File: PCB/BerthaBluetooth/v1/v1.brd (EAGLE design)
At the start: 111.9 x 84.6 mm, 112 parts, among them CON1 SPI, IC1 REG1117, J1 RJ12, J2 RJ12, J3 RJ12, J4 RJ12, J5 RJ12, J6 RJ12, Q1 BSP613P, Q10 BSP613P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

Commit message: Update labels
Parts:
- Q1, Q10, Q2, Q3, Q4, Q5, Q6, Q8, Q9: value BSP613P -> BSP75
- R25, R33, R5: value RJ12 -> 1k
- X4: value MINI-USB-SCHIELD-32005-201 -> MINI-USB

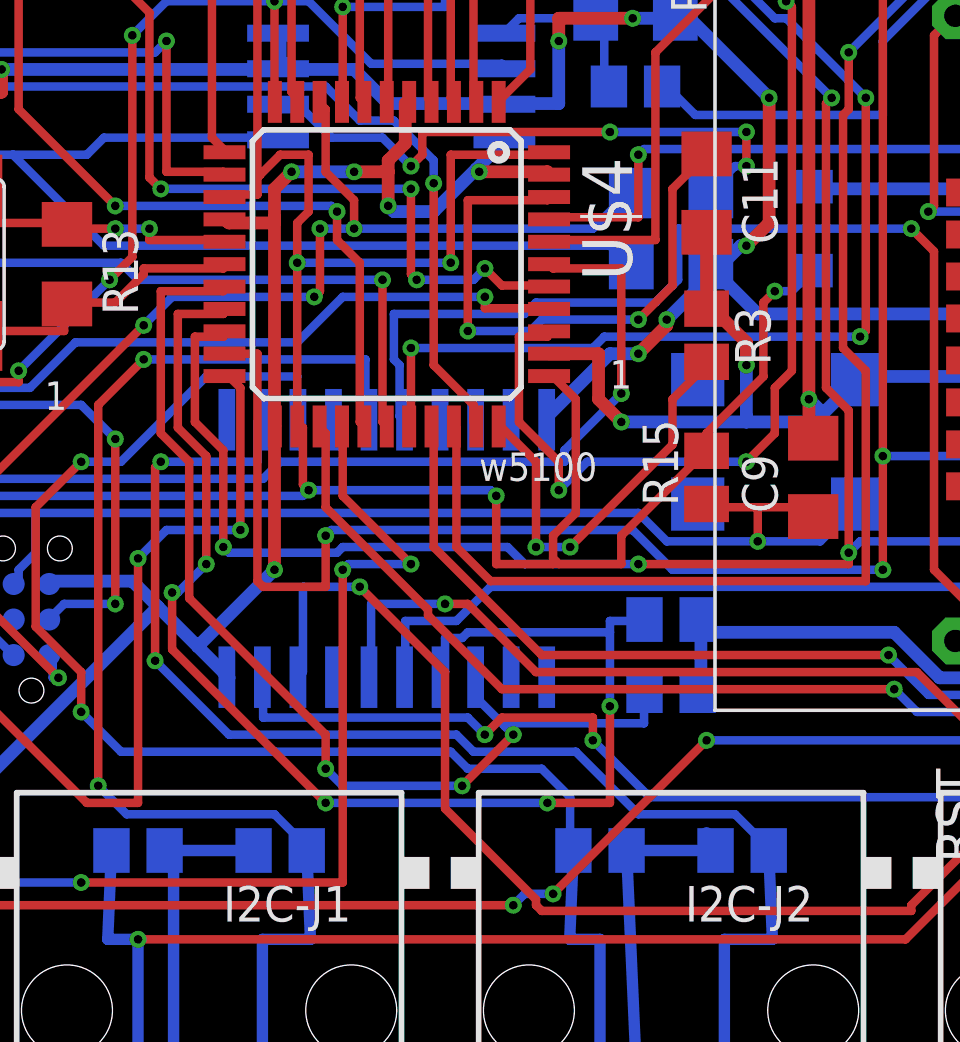
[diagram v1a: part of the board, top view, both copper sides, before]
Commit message: Update labels of sensor
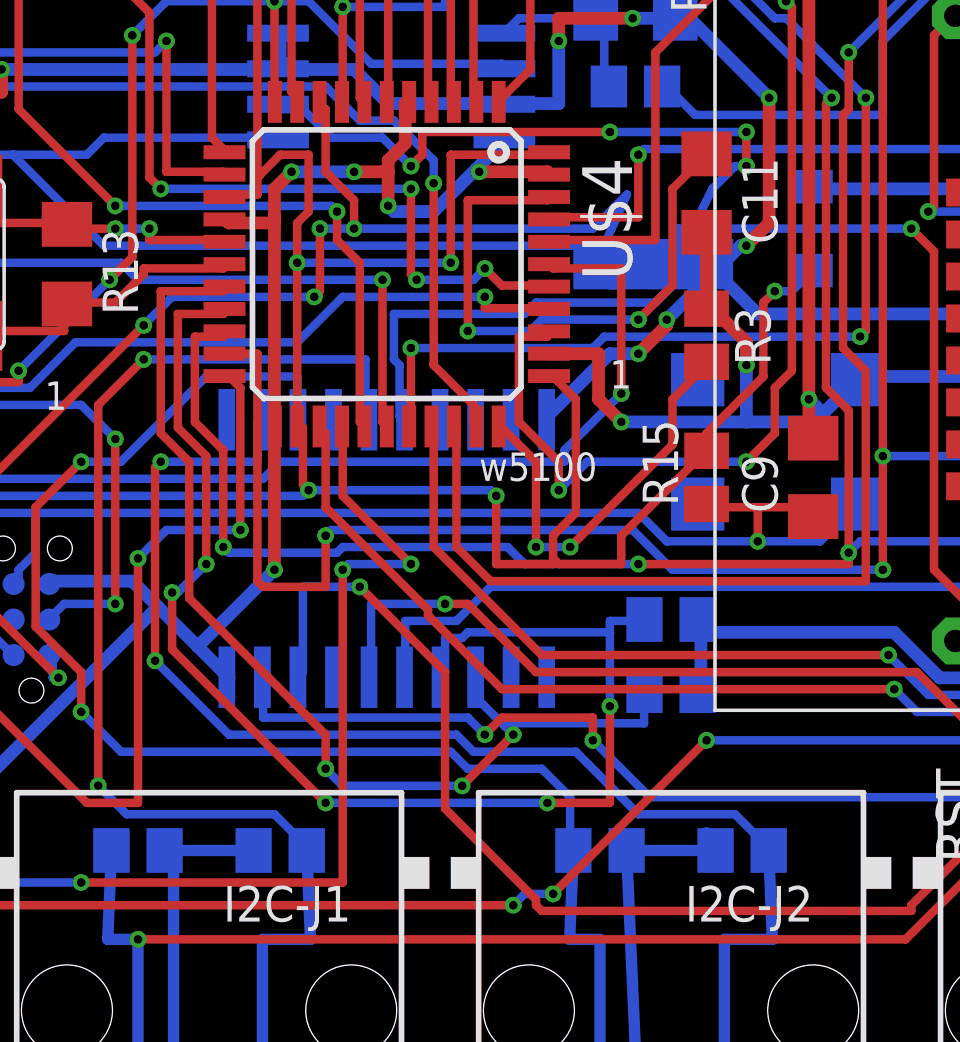
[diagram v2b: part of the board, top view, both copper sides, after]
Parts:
- moved R18 2.84 mm to (63.5, 39.4)
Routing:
- net N$23: track 21.6 -> 24.5 mm
- net SCK: track 40.6 -> 43.2 mm
- net +5V: track 659.8 -> 659.2 mm
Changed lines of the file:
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@@
 <layer number="23" name="tOrigins" color="15" fill="1" visible="yes" active="yes"/>
 <layer number="24" name="bOrigins" color="15" fill="1" visible="yes" active="yes"/>
-<layer number="25" name="tNames" color="7" fill="1" visible="no" active="yes"/>
-<layer number="26" name="bNames" color="7" fill="1" visible="no" active="yes"/>
-<layer number="27" name="tValues" color="7" fill="1" visible="no" active="yes"/>
+<layer number="25" name="tNames" color="7" fill="1" visible="yes" active="yes"/>
+<layer number="26" name="bNames" color="7" fill="1" visible="yes" active="yes"/>
+<layer number="27" name="tValues" color="7" fill="1" visible="yes" active="yes"/>
 <layer number="28" name="bValues" color="7" fill="1" visible="yes" active="yes"/>
-<layer number="29" name="tStop" color="7" fill="3" visible="no" active="yes"/>
-<layer number="30" name="bStop" color="7" fill="6" visible="no" active="yes"/>
-<layer number="31" name="tCream" color="7" fill="4" visible="no" active="yes"/>
-<layer number="32" name="bCream" color="7" fill="5" visible="no" active="yes"/>
-<layer number="33" name="tFinish" color="6" fill="3" visible="no" active="yes"/>
+<layer number="29" name="tStop" color="7" fill="3" visible="yes" active="yes"/>
+<layer number="30" name="bStop" color="7" fill="6" visible="yes" active="yes"/>
+<layer number="31" name="tCream" color="7" fill="4" visible="yes" active="yes"/>
+<layer number="32" name="bCream" color="7" fill="5" visible="yes" active="yes"/>
+<layer number="33" name="tFinish" color="6" fill="3" visible="yes" active="yes"/>
 <layer number="34" name="bFinish" color="6" fill="6" visible="yes" active="yes"/>
-<layer number="35" name="tGlue" color="7" fill="4" visible="no" active="yes"/>
-<layer number="36" name="bGlue" color="7" fill="5" visible="no" active="yes"/>
-<layer number="37" name="tTest" color="7" fill="1" visible="no" active="yes"/>
-<layer number="38" name="bTest" color="7" fill="1" visible="no" active="yes"/>
-<layer number="39" name="tKeepout" color="4" fill="11" visible="no" active="yes"/>
-<layer number="40" name="bKeepout" color="1" fill="11" visible="no" active="yes"/>
+<layer number="35" name="tGlue" color="7" fill="4" visible="yes" active="yes"/>
+<layer number="36" name="bGlue" color="7" fill="5" visible="yes" active="yes"/>
+<layer number="37" name="tTest" color="7" fill="1" visible="yes" active="yes"/>
+<layer number="38" name="bTest" color="7" fill="1" visible="yes" active="yes"/>
+<layer number="39" name="tKeepout" color="4" fill="11" visible="yes" active="yes"/>
+<layer number="40" name="bKeepout" color="1" fill="11" visible="yes" active="yes"/>
 <layer number="41" name="tRestrict" color="4" fill="10" visible="yes" active="yes"/>
 <layer number="42" name="bRestrict" color="1" fill="10" visible="yes" active="yes"/>
@@
 <layer number="45" name="Holes" color="7" fill="1" visible="no" active="yes"/>
 <layer number="46" name="Milling" color="3" fill="1" visible="no" active="yes"/>
-<layer number="47" name="Measures" color="7" fill="1" visible="no" active="yes"/>
-<layer number="48" name="Document" color="7" fill="1" visible="no" active="yes"/>
-<layer number="49" name="Reference" color="7" fill="1" visible="no" active="yes"/>
+<layer number="47" name="Measures" color="7" fill="1" visible="yes" active="yes"/>
+<layer number="48" name="Document" color="7" fill="1" visible="yes" active="yes"/>
+<layer number="49" name="Reference" color="7" fill="1" visible="yes" active="yes"/>
 <layer number="50" name="dxf" color="12" fill="1" visible="no" active="no"/>
-<layer number="51" name="tDocu" color="7" fill="1" visible="no" active="yes"/>
+<layer number="51" name="tDocu" color="7" fill="1" visible="yes" active="yes"/>
 <layer number="52" name="bDocu" color="7" fill="1" visible="yes" active="yes"/>
 <layer number="53" name="tGND_GNDA" color="7" fill="1" visible="no" active="no"/>
@@
 <attribute name="VALUE" x="64.77" y="44.7675" size="1.27" layer="28" rot="MR90"/>
 </element>
-<element name="R18" library="rcl" package="R1206" value="10k" x="64.77" y="41.91" smashed="yes" rot="MR180">
-<attribute name="NAME" x="63.5" y="40.64" size="1.27" layer="26" rot="MR180"/>
-<attribute name="VALUE" x="66.675" y="41.275" size="1.27" layer="28" rot="MR90"/>
+<element name="R18" library="rcl" package="R1206" value="10k" x="63.5" y="39.37" smashed="yes" rot="MR180">
+<attribute name="NAME" x="62.23" y="38.1" size="1.27" layer="26" rot="MR180"/>
+<attribute name="VALUE" x="65.405" y="38.735" size="1.27" layer="28" rot="MR90"/>
 </element>
 <element name="R" library="rcl" package="R0805" value="1k" x="23.495" y="76.2" rot="MR90"/>
@@
 <element name="R9" library="rcl" package="R0805" value="1.2K" x="72.39" y="50.8" rot="R270"/>
 <element name="R10" library="rcl" package="R0805" value="1K" x="63.5" y="50.8" rot="R270"/>
-<element name="C11" library="rcl" package="C1206" value="100nF" x="66.04" y="41.91" rot="R270"/>
+<element name="C11" library="rcl" package="C1206" value="100nF" x="66.04" y="41.91" smashed="yes" rot="R270">
+<attribute name="NAME" x="67.31" y="43.18" size="1.27" layer="25" rot="R270"/>
+<attribute name="VALUE" x="62.23" y="44.45" size="1.27" layer="27" rot="R270"/>
+</element>
 <element name="CON1" library="lpatiny" package="TC2030-MCP-NL" value="SPI" x="41.91" y="24.13" rot="MR90"/>
 <element name="C10" library="rcl" package="C1206" value="10uF" x="31.75" y="38.1" smashed="yes" rot="MR90">
@@
 </element>
 <element name="D5" library="lpatiny" package="LED-1206" value="1N581D1206" x="26.67" y="35.56" rot="MR180"/>
-<element name="R3" library="resistor" package="M0805" value="10k" x="66.04" y="36.83" rot="R270"/>
-<element name="R15" library="resistor" package="M0805" value="10k" x="66.04" y="31.75" rot="R90"/>
+<element name="R3" library="resistor" package="M0805" value="10k" x="66.04" y="36.83" smashed="yes" rot="R270">
+<attribute name="NAME" x="67.056" y="37.846" size="1.27" layer="25" rot="R270"/>
+<attribute name="VALUE" x="63.754" y="37.846" size="1.27" layer="27" rot="R270"/>
+</element>
+<element name="R15" library="resistor" package="M0805" value="10k" x="66.04" y="31.75" smashed="yes" rot="R90">
+<attribute name="NAME" x="65.024" y="30.734" size="1.27" layer="25" rot="R90"/>
+<attribute name="VALUE" x="64.8335" y="30.4165" size="1.27" layer="27" rot="R90"/>
+</element>
 <element name="C3" library="rcl" package="C1206" value="100nF" x="53.34" y="50.8"/>
 <element name="X3" library="lpatiny" package="NX6035" value="16MHz" x="39.37" y="39.37" smashed="yes" rot="R90">
@@
 <wire x1="94.93" y1="18.415" x2="98.11" y2="18.415" width="0.4064" layer="16"/>
 <wire x1="46.67" y1="18.415" x2="46.99" y2="18.415" width="0.4064" layer="16"/>
-<wire x1="46.99" y1="18.415" x2="46.99" y2="17.78" width="0.4064" layer="16"/>
 <wire x1="46.99" y1="17.78" x2="46.99" y2="8.255" width="0.4064" layer="16"/>
 <wire x1="46.99" y1="8.255" x2="46.355" y2="8.255" width="0.4064" layer="16"/>
@@
 <wire x1="63.1952" y1="41.8592" x2="61.976" y2="40.64" width="0.3048" layer="16"/>
 <wire x1="41.2496" y1="26.6192" x2="41.275" y2="26.67" width="0.3048" layer="16"/>
-<wire x1="63.1952" y1="41.8592" x2="63.348" y2="41.91" width="0.3048" layer="16"/>
+<wire x1="63.1952" y1="41.8592" x2="62.078" y2="39.37" width="0.3048" layer="16"/>
 <wire x1="52.4256" y1="44.9072" x2="52.2224" y2="45.1104" width="0.3048" layer="1"/>
 <wire x1="52.4256" y1="42.672" x2="52.4256" y2="44.9072" width="0.3048" layer="1"/>
@@
 <wire x1="51.6128" y1="44.9072" x2="52.6288" y2="43.8912" width="0.3048" layer="16"/>
 <wire x1="50.8" y1="44.9072" x2="51.6128" y2="44.9072" width="0.3048" layer="16"/>
-<wire x1="66.2432" y1="42.0624" x2="66.192" y2="41.91" width="0.3048" layer="16"/>
+<wire x1="66.2432" y1="42.0624" x2="64.922" y2="39.37" width="0.3048" layer="16"/>
 <wire x1="50.8" y1="44.9072" x2="50.7238" y2="45.085" width="0.3048" layer="16"/>
 <via x="67.4624" y="42.8752" extent="1-16" drill="0.3048"/>
@@
 <wire x1="66.04" y1="32.7152" x2="66.04" y2="33.3248" width="0.3048" layer="1"/>
 <wire x1="69.6976" y1="39.0144" x2="69.85" y2="39.14" width="0.3048" layer="16"/>
-<wire x1="66.04" y1="32.7152" x2="66.04" y2="32.7" width="0.3048" layer="1"/>
 <wire x1="61.3664" y1="34.544" x2="60.5536" y2="35.3568" width="0.3048" layer="1"/>
 <wire x1="61.3664" y1="30.48" x2="61.3664" y2="34.544" width="0.3048" layer="1"/>
